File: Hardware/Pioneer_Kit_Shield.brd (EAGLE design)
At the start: 53.3 x 59.7 mm, 38 parts, among them U1 USD-SOCKETNEW, U2 ARDUINO_UNO_R3_SHIELDNOLABELS, U3 HEX_CONVERTER, U4 PCA9306, U5 3.3V

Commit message: Final version before review
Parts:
- removed C3: 10uF, SparkFun-Capacitors:0603
- removed SJ1, SJ2: JUMPER-SMT_2_NC_PASTE_SILK, SparkFun-Jumpers:SMT-JUMPER_2_NC_PASTE_SILK
- added C7: 22pF, SparkFun-Capacitors:0603
- added D1: 3A/40V/500mV, SparkFun-DiscreteSemi:SMA-DIODE
- added FRAME2: FRAME-LETTERNO_PACKAGE, SparkFun-Aesthetics:DUMMY
- added J1: AMP FCI 10103594-0001LF, SparkFun-Connectors:USB-MICROB-PTH
- added L1: 1uH, SparkFun-Coils:INDUCTOR-SRP4020
- added R8: 180k, SparkFun-Resistors:0603
- added R9: 820k, SparkFun-Resistors:0603
- C5: value 1.0uF -> 10uF; device SparkFun-Capacitors:0603 -> SparkFun-Capacitors:0805
- C6: value 1.0uF -> 10uF
- U2: value ARDUINO_UNO_R3_SHIELDNOLABELS -> ARDUINO_UNO_R3_SHIELDUNO_R3_SHIELD_NOLABELS_LOCK; device SparkFun-Boards:UNO_R3_SHIELD_NOLABELS -> SparkFun-Boards:UNO_R3_SHIELD_NOLABELS_LOCK
- U5: value 3.3V -> TPS62065; device SparkFun-IC-Power:SOT23-5 -> SparkFun-IC-Power:WSON-8-PAD
- moved C1 51.9 mm to (40.6, 49.8)
- moved J2 50.1 mm to (27.9, 5.08), turned to 0 degrees
- moved C2 37.4 mm to (22.5, 39.1), turned to 90 degrees
- moved U1 32.5 mm to (39.4, 43.2), turned to 0 degrees
- moved R3 32.2 mm to (19.7, 12.7), turned to 270 degrees
- moved R2 29.9 mm to (21.3, 12.7), turned to 270 degrees
- moved C4 29.2 mm to (16.3, 10.0), turned to 180 degrees
- moved R6 26.7 mm to (9.40, 12.7), turned to 90 degrees
- moved U4 25.7 mm to (16.5, 12.7), turned to 90 degrees
- moved U3 25.0 mm to (26.0, 32.4), turned to 270 degrees
- moved JP1 24.5 mm to (25.9, 7.37)
- moved JP9 23.4 mm to (15.2, 15.2), turned to 180 degrees
- moved R4 23.1 mm to (12.7, 12.7), turned to 90 degrees
- moved R5 22.8 mm to (10.9, 12.7), turned to 90 degrees
- moved R7 11.4 mm to (9.14, 31.5)
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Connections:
- removed net D8: JP5.1, U2.D8
- removed net VDD: C6.1, JP8.1, U5.5
- new net !CD: JP5.1, U1.CD2, U2.D8
- new net N$20: C5.1, D1.C, J1.VBUS, U5.5, U5.7, U5.8
- new net N$31: C7.1, R8.2, R9.1, U5.4
- new net N$32: L1.P$1, U5.2
- new net SHIELD: J1.P$1, J1.P$10, J1.P$12, J1.P$2, J1.P$3, J1.P$4, J1.P$6, J1.P$8, J1.SHEILD2, J1.SHIELD, J1.SHIELD3, J1.SHIELD4
- new net VCC: C6.1, C7.2, JP8.1, L1.P$2, R9.2
- net 3.3V: no longer C3.1
- net 5V: now also D1.A; no longer C5.1, U5.1, U5.3
- net A4: no longer SJ1.2
- net A5: no longer SJ2.2
- net GND: now also J1.GND, R8.1, U5.1, U5.3, U5.6, U5.PAD; no longer C3.2, U1.CD1, U1.CD2, U5.2
- net RES: now also U2.RES
- net SCL: no longer SJ2.1
- net SDA: no longer SJ1.1
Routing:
- net SCL: track 73.8 -> 16.1 mm, vias 1 -> 0
- net SDA: track 64.5 -> 17.5 mm, vias 1 -> 0
- net N$20: track 0.00 -> 41.6 mm, vias 0 -> 2
- net !CD: track 0.00 -> 40.9 mm, vias 0 -> 2
- net GND: track 41.2 -> 2.11 mm
- net A4: track 43.9 -> 5.08 mm
- net A5: track 43.7 -> 5.08 mm
- net TX_LV: track 47.8 -> 15.1 mm, vias 2 -> 0
- net 3.3V: track 143.9 -> 173.7 mm, vias 6 -> 9
- net SHIELD: track 0.00 -> 28.0 mm, vias 0 -> 4
- net N$4: track 11.4 -> 35.0 mm
- net MISO: track 48.0 -> 69.9 mm, vias 0 -> 2
- net VDD: track 21.3 -> 0.00 mm, vias 2 -> 0
- net N$2: track 11.6 -> 30.0 mm, vias 2 -> 0
- net !CS: track 43.0 -> 26.5 mm
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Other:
- board text added: "5V/1A"
- board text added: "POW"
- board text added: "XBee DIO5"
- board text removed: "DIO5"
- board text removed: "Original uSD Shield design by R Owens and T Klopfenstein"
- board text removed: "PWR"

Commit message: Changes from review
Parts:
- S1, S2: device SparkFun:TACTILE_SWITCH_SMD -> SparkFun-Switches:TACTILE_SWITCH_SMD_5.2MM
- U3: value HEX_CONVERTER -> 74HC4050; device SparkFun:SO016 -> SparkFun-IC-Comms:SO16
- moved C7 1.55 mm to (35.2, 15.1)
- moved R8 1.55 mm to (32.1, 13.8)
- moved R9 1.55 mm to (33.7, 15.1)
- moved C5 1.55 mm to (25.7, 18.0)
- moved C6 1.55 mm to (30.7, 18.0)
- moved D1 1.55 mm to (28.2, 21.8)
- moved L1 1.55 mm to (28.2, 14.2)
- moved U5 1.55 mm to (28.2, 18.0)
- moved LED1 1.33 mm to (47.0, 8.00)
- moved R1 1.33 mm to (43.2, 8.00)
- moved J1 1.27 mm to (44.5, 2.92)
- moved JP8 1.27 mm to (26.7, 38.1)
- moved R2 1.27 mm to (22.6, 12.7)
- moved S1 1.27 mm to (49.5, 12.7)
- moved U1 1.27 mm to (40.6, 43.2)
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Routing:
- net SCK: track 29.3 -> 30.1 mm
- net MOSI: track 27.1 -> 27.8 mm
- net D9: track 62.5 -> 63.2 mm
- net D7: track 73.4 -> 74.1 mm
- net GND: track 2.11 -> 2.72 mm
- net TX_LV: track 15.1 -> 15.6 mm
- net N$2: track 30.0 -> 29.4 mm
- net N$163: track 26.0 -> 25.5 mm
- net !CS: track 26.5 -> 27.1 mm
- net N$4: track 35.0 -> 34.5 mm
- net 3.3V: vias 9 -> 11
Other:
- board text added: "IO REF"
- board text added: "Pioneer Add-on Shield"
- board text removed: "IOREF"

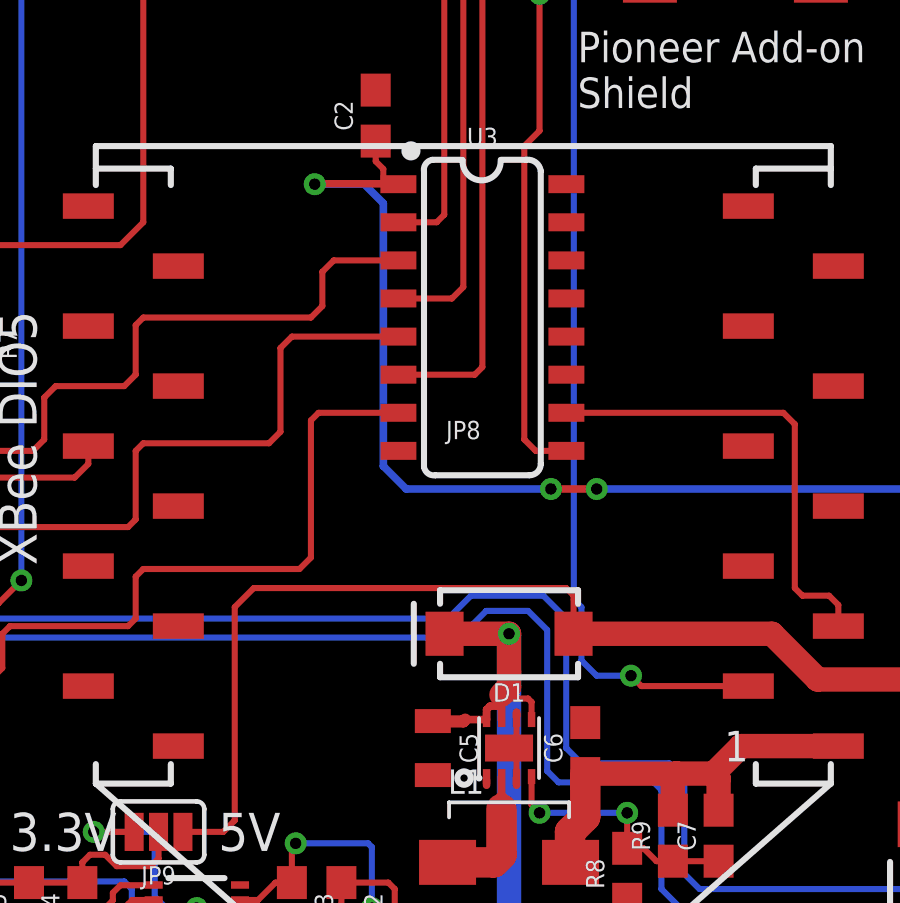
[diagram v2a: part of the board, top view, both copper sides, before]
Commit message: Fixed issues from QC double check
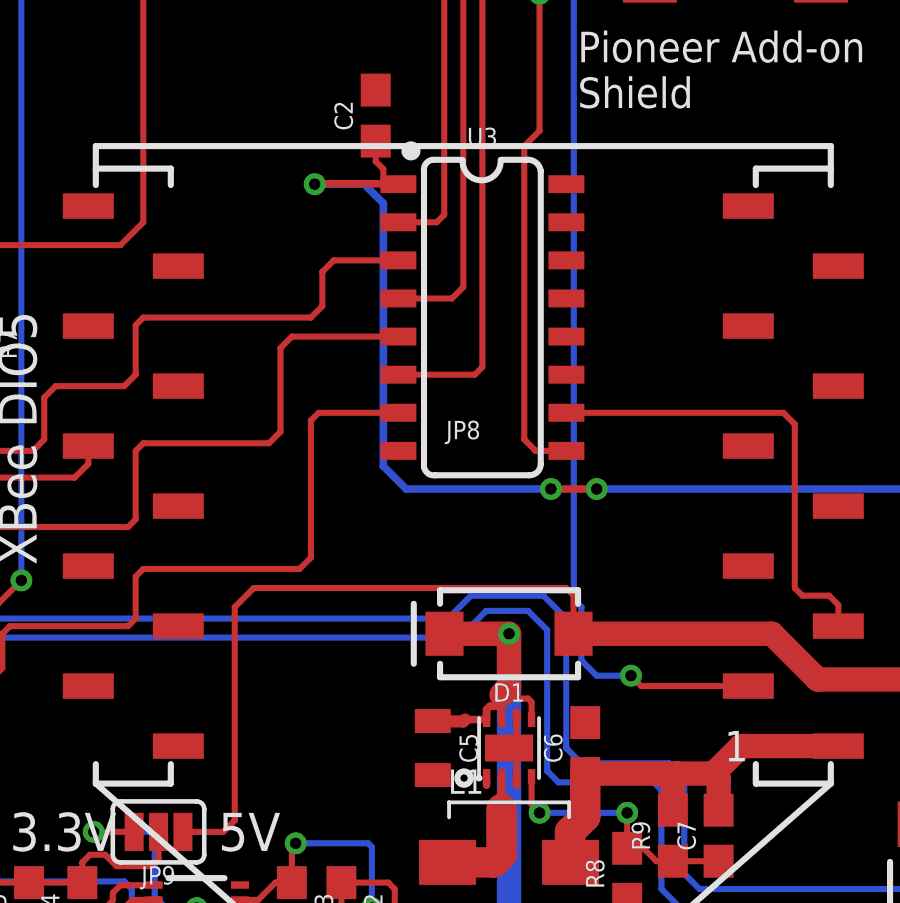
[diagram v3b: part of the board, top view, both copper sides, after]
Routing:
- net 3.3V: track 173.7 -> 174.2 mm
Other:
- board text added: "Dimensions in INCHES"
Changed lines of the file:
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@@
 <layers>
 <layer number="1" name="Top" color="4" fill="1" visible="yes" active="yes"/>
-<layer number="2" name="Route2" color="1" fill="3" visible="no" active="yes"/>
-<layer number="15" name="Route15" color="4" fill="6" visible="no" active="yes"/>
+<layer number="2" name="Route2" color="1" fill="3" visible="yes" active="yes"/>
+<layer number="15" name="Route15" color="4" fill="6" visible="yes" active="yes"/>
 <layer number="16" name="Bottom" color="1" fill="1" visible="yes" active="yes"/>
 <layer number="17" name="Pads" color="2" fill="1" visible="yes" active="yes"/>
@@
 <layer number="23" name="tOrigins" color="15" fill="1" visible="yes" active="yes"/>
 <layer number="24" name="bOrigins" color="15" fill="1" visible="yes" active="yes"/>
-<layer number="25" name="tNames" color="7" fill="1" visible="no" active="yes"/>
-<layer number="26" name="bNames" color="7" fill="1" visible="no" active="yes"/>
-<layer number="27" name="tValues" color="7" fill="1" visible="no" active="yes"/>
-<layer number="28" name="bValues" color="7" fill="1" visible="no" active="yes"/>
-<layer number="29" name="tStop" color="7" fill="3" visible="no" active="yes"/>
-<layer number="30" name="bStop" color="7" fill="6" visible="no" active="yes"/>
-<layer number="31" name="tCream" color="7" fill="4" visible="no" active="yes"/>
-<layer number="32" name="bCream" color="7" fill="5" visible="no" active="yes"/>
-<layer number="39" name="tKeepout" color="4" fill="11" visible="no" active="yes"/>
-<layer number="40" name="bKeepout" color="1" fill="11" visible="no" active="yes"/>
-<layer number="41" name="tRestrict" color="4" fill="10" visible="no" active="yes"/>
-<layer number="42" name="bRestrict" color="1" fill="10" visible="no" active="yes"/>
-<layer number="43" name="vRestrict" color="2" fill="10" visible="no" active="yes"/>
-<layer number="44" name="Drills" color="7" fill="1" visible="no" active="yes"/>
+<layer number="25" name="tNames" color="7" fill="1" visible="yes" active="yes"/>
+<layer number="26" name="bNames" color="7" fill="1" visible="yes" active="yes"/>
+<layer number="27" name="tValues" color="7" fill="1" visible="yes" active="yes"/>
+<layer number="28" name="bValues" color="7" fill="1" visible="yes" active="yes"/>
+<layer number="29" name="tStop" color="7" fill="3" visible="yes" active="yes"/>
+<layer number="30" name="bStop" color="7" fill="6" visible="yes" active="yes"/>
+<layer number="31" name="tCream" color="7" fill="4" visible="yes" active="yes"/>
+<layer number="32" name="bCream" color="7" fill="5" visible="yes" active="yes"/>
+<layer number="39" name="tKeepout" color="4" fill="11" visible="yes" active="yes"/>
+<layer number="40" name="bKeepout" color="1" fill="11" visible="yes" active="yes"/>
+<layer number="41" name="tRestrict" color="4" fill="10" visible="yes" active="yes"/>
+<layer number="42" name="bRestrict" color="1" fill="10" visible="yes" active="yes"/>
+<layer number="43" name="vRestrict" color="2" fill="10" visible="yes" active="yes"/>
+<layer number="44" name="Drills" color="7" fill="1" visible="yes" active="yes"/>
 <layer number="45" name="Holes" color="7" fill="1" visible="yes" active="yes"/>
-<layer number="46" name="Milling" color="3" fill="1" visible="no" active="yes"/>
+<layer number="46" name="Milling" color="3" fill="1" visible="yes" active="yes"/>
 <layer number="47" name="Measures" color="7" fill="1" visible="yes" active="yes"/>
-<layer number="48" name="Document" color="7" fill="1" visible="no" active="yes"/>
-<layer number="49" name="Reference" color="7" fill="1" visible="no" active="yes"/>
+<layer number="48" name="Document" color="7" fill="1" visible="yes" active="yes"/>
+<layer number="49" name="Reference" color="7" fill="1" visible="yes" active="yes"/>
 <layer number="51" name="tDocu" color="6" fill="1" visible="yes" active="yes"/>
-<layer number="52" name="bDocu" color="7" fill="1" visible="no" active="yes"/>
+<layer number="52" name="bDocu" color="7" fill="1" visible="yes" active="yes"/>
 <layer number="3" name="Route3" color="4" fill="3" visible="no" active="no"/>
 <layer number="4" name="Route4" color="1" fill="4" visible="no" active="no"/>
@@
 <text x="30.48" y="39.37" size="1.016" layer="21" font="vector" ratio="15">Pioneer Add-on
 Shield</text>
+<text x="30.48" y="-16.51" size="1.778" layer="47" font="vector" ratio="15">Dimensions in INCHES</text>
 </plain>
 <attributes>
@@
 <wire x1="24.003" y1="36.8427" x2="21.7297" y2="36.8427" width="0.254" layer="1"/>
 <wire x1="21.7297" y1="36.8427" x2="21.717" y2="36.83" width="0.254" layer="1"/>
-<wire x1="24.003" y1="36.8427" x2="24.505" y2="36.83" width="0" layer="19" extent="1-1"/>
+<wire x1="24.003" y1="36.8427" x2="24.4923" y2="36.8427" width="0.254" layer="1"/>
+<wire x1="24.4923" y1="36.8427" x2="24.505" y2="36.83" width="0.254" layer="1"/>
 </signal>
 <signal name="GND">
@@
 <wire x1="28.444" y1="17.054" x2="28.444" y2="16.794" width="0.254" layer="1"/>
 <wire x1="28.448" y1="19.05" x2="28.448" y2="19.234" width="0.254" layer="1"/>
-<wire x1="28.444" y1="18.984" x2="28.448" y2="19.05" width="0" layer="19" extent="1-1"/>
+<wire x1="28.444" y1="18.984" x2="28.444" y2="19.046" width="0.254" layer="1"/>
+<wire x1="28.444" y1="19.046" x2="28.448" y2="19.05" width="0.254" layer="1"/>
 </signal>
 <signal name="N$6">
